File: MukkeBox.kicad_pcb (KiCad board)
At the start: 2 copper layers, 200 x 105 mm, 272 parts, among them J101 Conn_02x20_Odd_Even, J102 Conn_01x04, J103 Conn_02x05_Odd_Even, J104 Conn_02x05_Odd_Even, J301 Conn_02x04_Odd_Even, J302 Conn_02x04_Odd_Even, J303 TB001-500-02BE CUI_Devices, J401 TB001-500-02BE CUI_Devices, J501 TB001-500-04BE CUI_Devices, J601 Conn_01x03_Female, J602 Conn_02x01, J603 Conn_02x06_Odd_Even, J604 Conn_02x01, J605 Conn_02x01, Q1 2N7002, Q201 VS6412AE, Q202 VS6412AE, Q301 2N7002, Q302 HSBB3103, Q303 2N7002, Q304 HSBB3103, Q305 VS6412AE, Q306 2N7002, Q307 BSS84, Q308 2N7002, Q309 VS6412AE, Q310 HSBB3103, Q311 HSBB3103, Q501 2N7002, SW501 DS04-254-2-02BK-SMT, U101 LM35-LP, U102 STM32F030C6Tx_MukkeBox, U202 StepUp, U203 TPS40210, U301 BQ24610, U501 TDA7498L, U502 BK8000L, U503 TDA7719, U504 AP2553AW6-7, U601 XC6216C, U602 TPS560430, Y101 FOXSDLF/080-20

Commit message: Änderungen Arbeit hinzugefügt: Layout neuer Charger
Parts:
- removed Q202: VS6412AE, Package_SON:Diodes_PowerDI3333-8
- R_FBB601: value 22K1 -> 20K
- R_FBT601: value 51K -> 47K
- moved D201 115.6 mm to (141.5, 88.3), turned to 90 degrees
- moved D601 92.2 mm to (65.1, 94.3), turned to 180 degrees
- moved Q311 85.9 mm to (98.6, 67.7), turned to 90 degrees
- moved RSR301 83.7 mm to (86.3, 64.5), turned to 270 degrees
- moved Q310 80.6 mm to (87.2, 69.3), turned to 180 degrees
- moved C313 78.6 mm to (83.8, 64.6), turned to 270 degrees
- moved R15C301 78.5 mm to (91.9, 68.3), turned to 270 degrees
- moved C15C301 78.4 mm to (90.3, 68.3), turned to 270 degrees
- moved R8C301 75.7 mm to (74.0, 63.0), turned to 90 degrees
- moved R19C301 75.6 mm to (94.4, 67.4)
- moved C307 75.5 mm to (79.7, 59.9)
- moved C312 73.9 mm to (83.8, 61.2), turned to 270 degrees
- moved C314 73.8 mm to (80.3, 64.0)
- moved R2C301 72.3 mm to (80.3, 62.4)
- moved R3C301 70.8 mm to (72.3, 59.5), turned to 90 degrees
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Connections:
- D301 pad 1: Net-(D301-Pad1) -> (no net)
- J101 pad 27: Net-(J101-Pad27) -> (no net)
- J101 pad 32: Net-(J101-Pad32) -> (no net)
- J103 pad 10: Net-(J103-Pad10) -> (no net)
- J103 pad 5: Net-(J103-Pad5) -> (no net)
- J103 pad 9: Net-(J103-Pad9) -> (no net)
- R203 pad 2: Net-(Q202-Pad4) -> Net-(Q201-Pad4)
- U102 pad 39: ENABLE_12V -> (no net)
- U203 pad 3: Net-(U203-Pad3) -> (no net)
- U301 pad 17: Net-(U301-Pad17) -> GND
- U501 pad 25: Net-(U501-Pad25) -> (no net)
- U502 pad 12: Net-(U502-Pad12) -> (no net)
- U502 pad 13: Net-(U502-Pad13) -> (no net)
- U502 pad 14: Net-(U502-Pad14) -> (no net)
- U502 pad 15: Net-(U502-Pad15) -> (no net)
- U502 pad 17: Net-(U502-Pad17) -> (no net)
- U502 pad 18: Net-(U502-Pad18) -> (no net)
- U502 pad 19: Net-(U502-Pad19) -> (no net)
- U502 pad 2: Net-(U502-Pad2) -> (no net)
- U502 pad 20: Net-(U502-Pad20) -> (no net)
- U502 pad 21: Net-(U502-Pad21) -> (no net)
- U502 pad 22: Net-(U502-Pad22) -> (no net)
- U502 pad 23: Net-(U502-Pad23) -> (no net)
- U502 pad 28: Net-(U502-Pad28) -> (no net)
- U502 pad 30: Net-(U502-Pad30) -> (no net)
- U502 pad 31: Net-(U502-Pad31) -> (no net)
- U502 pad 4: Net-(U502-Pad4) -> (no net)
- U502 pad 5: Net-(U502-Pad5) -> (no net)
- U502 pad 6: Net-(U502-Pad6) -> (no net)
- U502 pad 7: Net-(U502-Pad7) -> (no net)
- U502 pad 9: Net-(U502-Pad9) -> (no net)
- U503 pad 19: Net-(U503-Pad19) -> (no net)
- U503 pad 20: Net-(U503-Pad20) -> (no net)
- U503 pad 4: Net-(U503-Pad4) -> (no net)
- U503 pad 5: Net-(U503-Pad5) -> (no net)
- U503 pad 6: Net-(U503-Pad6) -> (no net)
- U503 pad 7: Net-(U503-Pad7) -> (no net)
- U503 pad 8: Net-(U503-Pad8) -> (no net)
- U503 pad 9: Net-(U503-Pad9) -> (no net)
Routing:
- net CHARGER_STAT1: track 0.00 -> 92.3 mm, vias 0 -> 4
- net CHARGER_PG: track 0.00 -> 82.2 mm, vias 0 -> 4
- net CHARGER_STAT2: track 0.00 -> 78.6 mm, vias 0 -> 4
- net CHARGER_IOUT: track 70.3 -> 0.00 mm, vias 2 -> 0
- net PWR_EN: track 70.9 -> 33.9 mm
- net Net-(R19C301-Pad2): track 0.00 -> 34.5 mm, vias 0 -> 2
- net /00_Charger/VREF: track 0.00 -> 25.0 mm, vias 0 -> 2
- net /00_Charger/CE: track 0.00 -> 23.6 mm
- net /00_Charger/POWER_SUPPLY: track 20.7 -> 0.00 mm, vias 2 -> 0
- net +3V3: track 323.1 -> 340.0 mm
- net Net-(C314-Pad1): track 0.00 -> 16.8 mm
- net Net-(Q309-Pad1): track 16.4 -> 0.00 mm
- net Net-(Q309-Pad4): track 0.00 -> 15.3 mm, vias 0 -> 2
- net Net-(Q304-Pad3): track 14.4 -> 0.00 mm
- net Net-(R5C301-Pad1): track 0.00 -> 13.0 mm, vias 0 -> 2
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- added copper zone on F.Cu, net Net-(C15C301-Pad2)
- added copper zone on F.Cu, net Net-(C301-Pad2)
- added copper zone on F.Cu, net Net-(C303-Pad2)
- added copper zone on F.Cu, net Net-(D201-Pad1)
- removed copper zone on F.Cu, net /00_Charger/POWER_SUPPLY
- removed copper zone on F.Cu, net Net-(C412-Pad1)
- removed copper zone on F.Cu, net Net-(HS302-Pad1)

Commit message: Layout fertig, Schaltplan erneut checken
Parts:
- J303: value TB001-500-02BE CUI_Devices -> TB001-500-04BE CUI_Devices; footprint TerminalBlock_RND:TerminalBlock_RND_205-00045_1x02_P5.00mm_Horizontal -> TerminalBlock_RND:TerminalBlock_RND_205-00047_1x04_P5.00mm_Horizontal
- moved J301 23.5 mm to (108.2, 43.2), turned to 0 degrees
- moved C_5_2 21.4 mm to (107.2, 76.3), turned to 270 degrees
- moved U202 20.6 mm to (97.0, 42.9)
- moved R310 20.4 mm to (104.3, 53.7), turned to 90 degrees
- moved Q311 18.6 mm to (102.4, 49.5), turned to 0 degrees
- moved R307 18.4 mm to (102.6, 53.7), turned to 270 degrees
- moved L301 14.6 mm to (128.0, 60.3), turned to 0 degrees
- moved R512 10.8 mm to (156.8, 110.3), turned to 180 degrees
- moved J303 9.96 mm to (50.1, 88.3)
- moved R5 8.85 mm to (156.8, 107.7), turned to 180 degrees
- moved C15C301 8.72 mm to (98.1, 72.2), turned to 90 degrees
- moved Q310 8.13 mm to (95.1, 67.4)
- moved R4 8.01 mm to (156.8, 105.2), turned to 180 degrees
- moved R15C301 6.03 mm to (96.5, 72.2), turned to 90 degrees
- moved R19C301 5.71 mm to (94.0, 73.1), turned to 180 degrees
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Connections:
- C305 pad 2: Net-(C305-Pad2) -> /00_Charger/TS
- D301 pad 1: (no net) -> Net-(D301-Pad1)
- J101 pad 27: (no net) -> Net-(J101-Pad27)
- J101 pad 32: (no net) -> Net-(J101-Pad32)
- J103 pad 10: (no net) -> Net-(J103-Pad10)
- J103 pad 5: (no net) -> Net-(J103-Pad5)
- J103 pad 9: (no net) -> Net-(J103-Pad9)
- J303 pad 2: Net-(F301-Pad1) -> /00_Charger/TS
- L301 pad 3: (no net) -> GND
- R9C301 pad 1: Net-(C305-Pad2) -> /00_Charger/TS
- R9C302 pad 2: Net-(C305-Pad2) -> /00_Charger/TS
- U102 pad 39: (no net) -> Net-(U102-Pad39)
- U203 pad 3: (no net) -> Net-(U203-Pad3)
- U301 pad 25: (no net) -> GND
- U301 pad 6: Net-(C305-Pad2) -> /00_Charger/TS
- U501 pad 25: (no net) -> Net-(U501-Pad25)
- U502 pad 12: (no net) -> Net-(U502-Pad12)
- U502 pad 13: (no net) -> Net-(U502-Pad13)
- U502 pad 14: (no net) -> Net-(U502-Pad14)
- U502 pad 15: (no net) -> Net-(U502-Pad15)
- U502 pad 17: (no net) -> Net-(U502-Pad17)
- U502 pad 18: (no net) -> Net-(U502-Pad18)
- U502 pad 19: (no net) -> Net-(U502-Pad19)
- U502 pad 2: (no net) -> Net-(U502-Pad2)
- U502 pad 20: (no net) -> Net-(U502-Pad20)
- U502 pad 21: (no net) -> Net-(U502-Pad21)
- U502 pad 22: (no net) -> Net-(U502-Pad22)
- U502 pad 23: (no net) -> Net-(U502-Pad23)
- U502 pad 28: (no net) -> Net-(U502-Pad28)
- U502 pad 30: (no net) -> Net-(U502-Pad30)
- U502 pad 31: (no net) -> Net-(U502-Pad31)
- U502 pad 4: (no net) -> Net-(U502-Pad4)
- U502 pad 5: (no net) -> Net-(U502-Pad5)
- U502 pad 6: (no net) -> Net-(U502-Pad6)
- U502 pad 7: (no net) -> Net-(U502-Pad7)
- U502 pad 9: (no net) -> Net-(U502-Pad9)
- U503 pad 19: (no net) -> Net-(U503-Pad19)
- U503 pad 20: (no net) -> Net-(U503-Pad20)
- U503 pad 4: (no net) -> Net-(U503-Pad4)
- U503 pad 5: (no net) -> Net-(U503-Pad5)
- U503 pad 6: (no net) -> Net-(U503-Pad6)
- U503 pad 7: (no net) -> Net-(U503-Pad7)
- U503 pad 8: (no net) -> Net-(U503-Pad8)
- U503 pad 9: (no net) -> Net-(U503-Pad9)
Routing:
- net /00_Charger/TS: track 0.00 -> 57.4 mm, vias 0 -> 2
- net GND: track 23.4 -> 61.8 mm, vias 68 -> 97
- net SYSTEM_LOAD: track 207.1 -> 236.3 mm
- net Net-(Q306-Pad3): track 2.50 -> 27.9 mm
- net /02_StepUp/IN_STEPUP: track 46.4 -> 34.0 mm
- net Net-(C305-Pad2): track 9.64 -> 0.00 mm
- net Net-(C15C301-Pad1): track 5.21 -> 14.0 mm, vias 0 -> 2
- net Net-(C15C301-Pad2): track 12.9 -> 19.2 mm
- net DC_20V_POWER_SUPPLY: track 67.8 -> 73.9 mm
- net Net-(C307-Pad2): track 4.84 -> 9.75 mm, vias 0 -> 2
- net /StepDown/3V3_ON_OFF: track 2.01 -> 5.58 mm
- net Net-(R19C301-Pad2): track 34.5 -> 31.0 mm
- net PACK+: track 107.6 -> 110.2 mm
- net +3V3: track 340.0 -> 338.6 mm
- net PACK_SENSE: track 36.4 -> 37.7 mm
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
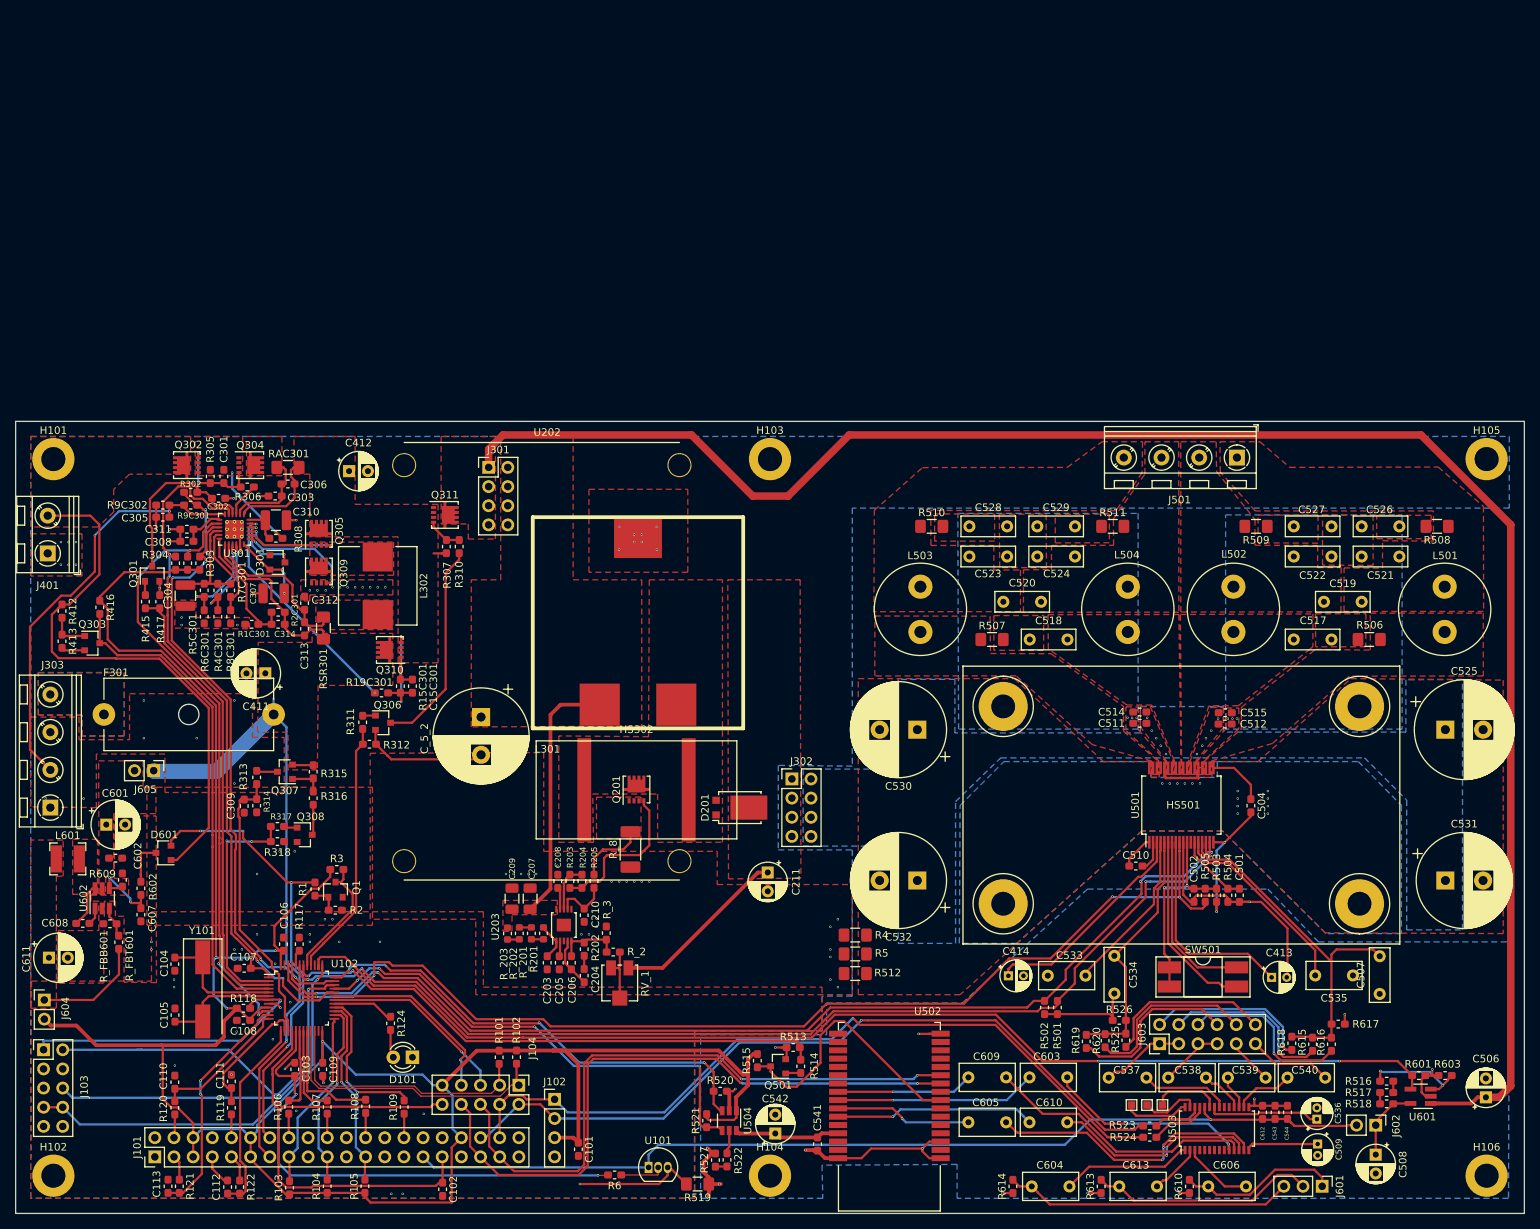
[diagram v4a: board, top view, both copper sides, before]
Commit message: Änderungen von der Arbeit, Viele LCSC Teile für teurere ausgetauscht
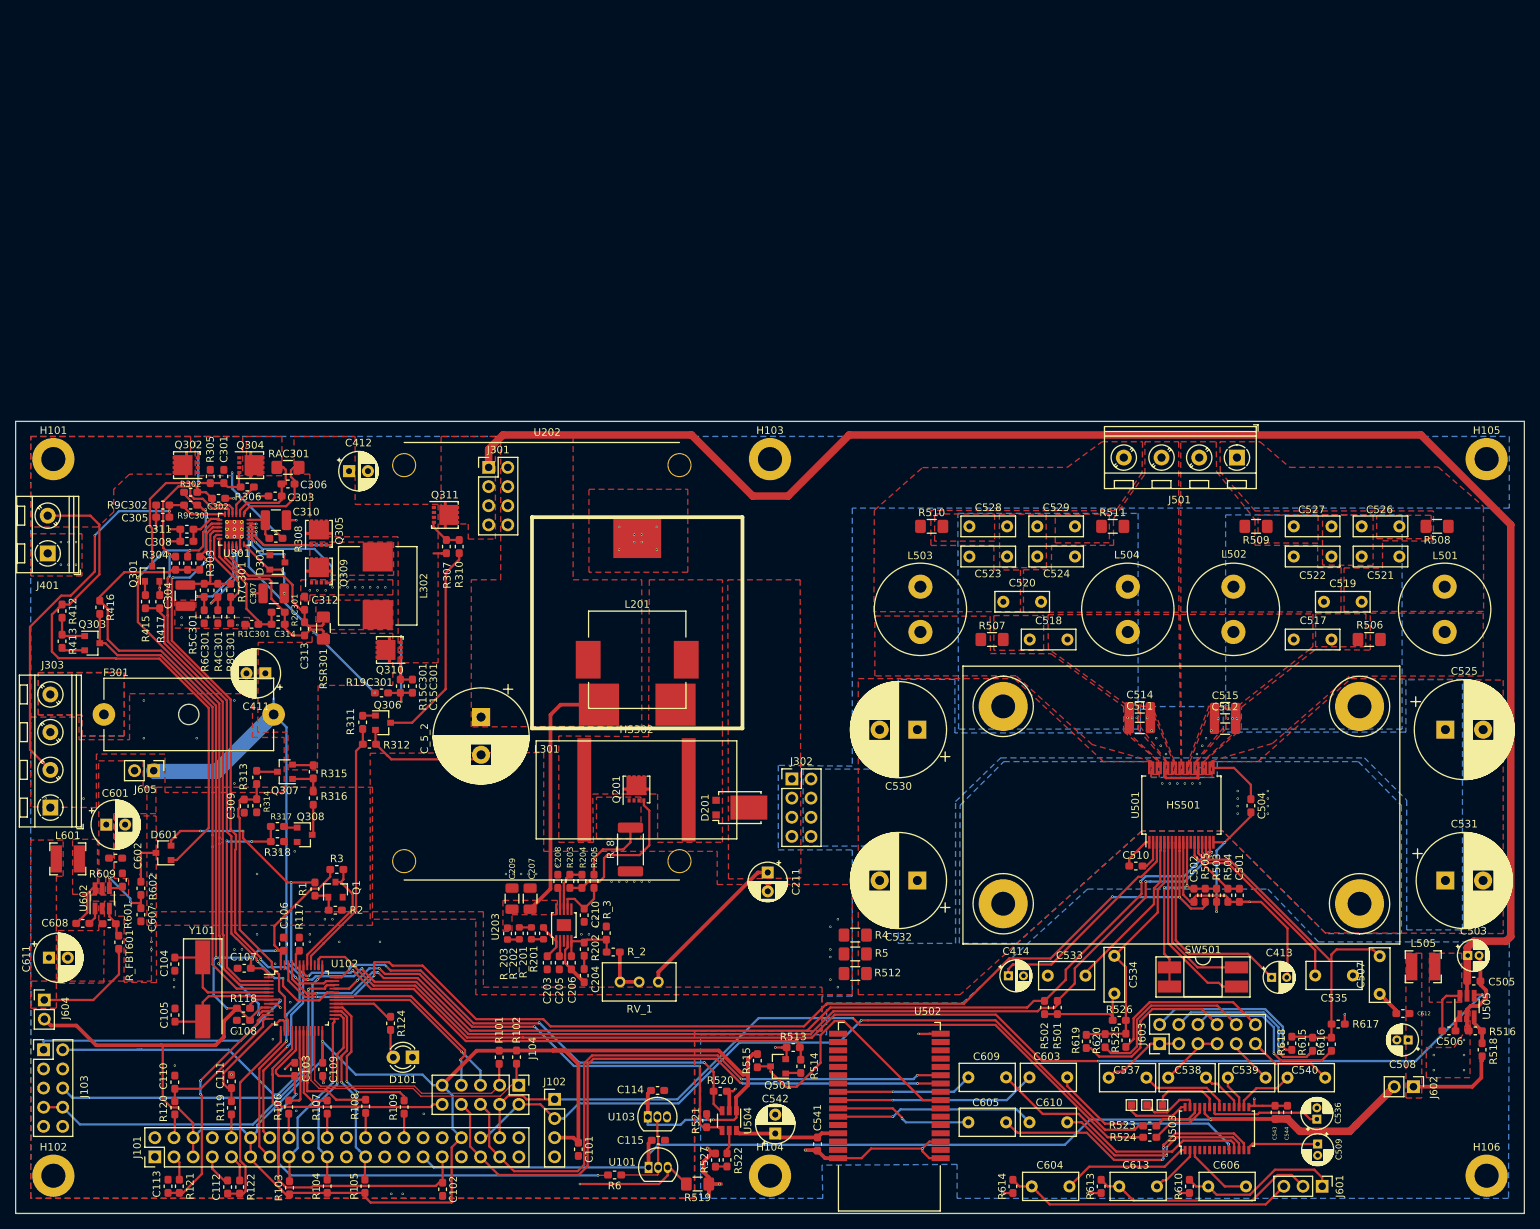
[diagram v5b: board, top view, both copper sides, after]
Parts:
- removed R517, R603: 10K, Resistor_SMD:R_0603_1608Metric_Pad1.05x0.95mm_HandSolder
- removed R_FBB601: 20K, Resistor_SMD:R_0603_1608Metric_Pad1.05x0.95mm_HandSolder
- removed U601: XC6216C, Package_TO_SOT_SMD:SOT-23-5_HandSoldering
- added C114: 100nF, Capacitor_SMD:C_0603_1608Metric_Pad1.05x0.95mm_HandSolder, F.Cu at (130.6, 125.8)
- added C115: 100nF, Capacitor_SMD:C_0603_1608Metric_Pad1.05x0.95mm_HandSolder, F.Cu at (130.7, 132.4)
- added C503: 2.2u, Capacitor_THT:CP_Radial_D4.0mm_P1.50mm, F.Cu at (238.0, 107.9)
- added C505: 100nF, Capacitor_SMD:C_0603_1608Metric_Pad1.05x0.95mm_HandSolder, F.Cu at (238.8, 111.3)
- added L201: 22uH TAITEC TMPC1265HP-220MG-D, Inductor_SMD:TAITEC TMPC1265HP-220MG-D, F.Cu at (127.9, 68.7)
- added L505: 10u Bourns SRN4018, Inductor_SMD:L_Bourns-SRN4018, F.Cu at (232.1, 109.4)
- added U103: MCP9700, Package_TO_SOT_THT:TO-92_Inline, F.Cu at (129.3, 129.3)
- added U505: JW5026, Package_TO_SOT_SMD:SOT-23-6_Handsoldering, F.Cu at (237.9, 114.6)
- C506: value 10u -> 100nF; footprint Capacitor_THT:CP_Radial_D5.0mm_P2.50mm -> Capacitor_SMD:C_0603_1608Metric_Pad1.05x0.95mm_HandSolder
- C508: footprint Capacitor_THT:CP_Radial_D5.0mm_P2.50mm -> Capacitor_THT:CP_Radial_D4.0mm_P1.50mm
- C511, C512, C514, C515: footprint Capacitor_SMD:C_0603_1608Metric_Pad1.05x0.95mm_HandSolder -> Capacitor_SMD:C_1210_3225Metric
- R516: value 10K -> 1K
- R601: value 10K -> 3K3
- R610: value 100K -> 100R
- RV_1: footprint Potentiometer_SMD:Potentiometer_Bourns_3314J_Vertical -> Potentiometer_THT:Potentiometer_Bourns_3296W_Vertical
- R_8: value R007 -> R012; footprint Resistor_SMD:R_2010_5025Metric_Pad1.52x2.65mm_HandSolder -> Resistor_SMD:R_2512_6332Metric
- R_FBT601: value 47K -> 10K
- U602: value TPS560430 -> JW5026
- moved R601 174.8 mm to (57.9, 103.7)
- moved C612 22.8 mm to (229.4, 115.6), turned to 180 degrees
- moved C508 15.8 mm to (230.1, 119.1), turned to 180 degrees
- moved R518 14.5 mm to (239.9, 120.4), turned to 90 degrees
- moved R516 13.5 mm to (239.0, 117.9)
- moved C506 10.1 mm to (235.5, 117.9), turned to 0 degrees
- moved J602 7.14 mm to (230.8, 125.3)
- moved RV_1 5.12 mm to (130.7, 111.4)
- moved L301 0.10 mm to (127.9, 60.3)
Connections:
- net Net-(R6-Pad1) renamed /S2
- C506 pad 1: SYSTEM_LOAD -> Net-(C506-Pad1)
- C506 pad 2: GNDA -> Net-(C506-Pad2)
- C612 pad 1: +8V -> Net-(C508-Pad1)
- R516 pad 2: Net-(R516-Pad2) -> GNDA
- R518 pad 2: Net-(R517-Pad2) -> Net-(R516-Pad1)
- R601 pad 1: ENABLE_8V -> GND
- R601 pad 2: GNDA -> Net-(R601-Pad2)
- R_FBT601 pad 1: Net-(R_FBB601-Pad2) -> Net-(R601-Pad2)
- U602 pad 3: Net-(R_FBB601-Pad2) -> Net-(R601-Pad2)
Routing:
- net SYSTEM_LOAD: track 236.3 -> 217.7 mm
- net Net-(R516-Pad2): track 14.1 -> 0.00 mm, vias 2 -> 0
- net +3V3: track 338.6 -> 352.3 mm, vias 5 -> 6
- net +8V: track 130.4 -> 141.9 mm
- net ENABLE_8V: track 157.9 -> 169.3 mm
- net GNDA: track 106.1 -> 115.4 mm, vias 15 -> 19
- net /S2: track 5.84 -> 12.6 mm
- net Net-(C506-Pad1): track 0.00 -> 6.67 mm
- net Net-(R_FBB601-Pad2): track 4.11 -> 0.00 mm
- net Net-(R601-Pad2): track 0.00 -> 4.11 mm
- net Net-(R516-Pad1): track 1.50 -> 4.01 mm
- net Net-(C211-Pad1): track 23.7 -> 21.3 mm
- net Net-(C508-Pad1): track 9.99 -> 12.4 mm
- net Net-(C506-Pad2): track 0.00 -> 2.19 mm
- net Net-(R517-Pad2): track 1.50 -> 0.00 mm
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- added copper zone on F.Cu, net GNDA
- added copper zone on F.Cu, net Net-(C506-Pad1)
- added copper zone on F.Cu, net Net-(C508-Pad1)
